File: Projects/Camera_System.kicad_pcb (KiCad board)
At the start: 2 copper layers, 67 x 98 mm, 63 parts, among them CON1 AVR-ISP-10, J1 BARREL_JACK, U1 IFX1117ME_V33, U10 RT1105AF160Q, U11 RT1105AF160Q, U12 LCD_1602, U13 RT1105AF160Q, U14 Si501, U15 OV7670-nofifo, U16 ESP8266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

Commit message: bom
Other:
- board size 67 x 98 mm -> 68 x 98 mm
- board text added: "A"
- board text added: "B"
- board text added: "CAMERA"
- board text added: "DISPLAY"
- board text added: "RST"
- board text added: "SD CARD"
- board text added: "WIFI"
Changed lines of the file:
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@@
     (links 191)
     (no_connects 0)
-    (area 52.324999 29.324999 271.775001 190.425001)
+    (area 40.024999 -48.28 278.375001 195.150001)
     (thickness 1.6)
-    (drawings 11)
+    (drawings 20)
     (tracks 659)
     (zones 0)
@@
     (visible_elements 7FFFFFFF)
     (pcbplotparams
-      (layerselection 0x00030_80000001)
+      (layerselection 0x01030_80000001)
       (usegerberextensions false)
       (excludeedgelayer true)
@@
       (psnegative false)
       (psa4output false)
-      (plotreference true)
-      (plotvalue true)
+      (plotreference false)
+      (plotvalue false)
       (plotinvisibletext false)
       (padsonsilk false)
@@
       (outputformat 1)
       (mirror false)
-      (drillshape 1)
+      (drillshape 0)
       (scaleselection 1)
-      (outputdirectory ""))
+      (outputdirectory Manufacturing/))
   )
   (net 0 "")
@@
     (tags "resistor 0603")
     (attr smd)
-    (fp_text reference R13 (at 0 -1.45) (layer F.SilkS)
+    (fp_text reference R13 (at 0.127 -1.524) (layer F.SilkS)
       (effects (font (size 1 1) (thickness 0.15)))
     )
@@
     (tags "resistor 0603")
     (attr smd)
-    (fp_text reference R10 (at 0 -1.45) (layer F.SilkS)
+    (fp_text reference R10 (at -0.081 1.546) (layer F.SilkS)
       (effects (font (size 1 1) (thickness 0.15)))
     )
@@
     (tags "resistor 0603")
     (attr smd)
-    (fp_text reference R9 (at 0 -1.45) (layer F.SilkS)
+    (fp_text reference R9 (at -0.208 -1.446) (layer F.SilkS)
       (effects (font (size 1 1) (thickness 0.15)))
     )
@@
     (tags "resistor 0603")
     (attr smd)
-    (fp_text reference R4 (at 0 -1.45 180) (layer F.SilkS)
+    (fp_text reference R4 (at 0.093 -1.858 180) (layer F.SilkS)
       (effects (font (size 1 1) (thickness 0.15)))
     )
@@
     (tags "resistor 0603")
     (attr smd)
-    (fp_text reference R2 (at 0 -1.45 270) (layer F.SilkS)
+    (fp_text reference R2 (at -0.351 -1.912 270) (layer F.SilkS)
       (effects (font (size 1 1) (thickness 0.15)))
     )
@@
     (tags "LED led 0603 SMD smd SMT smt smdled SMDLED smtled SMTLED")
     (attr smd)
-    (fp_text reference D3 (at 0 -1.25) (layer F.SilkS)
+    (fp_text reference D3 (at 0.13 1.858) (layer F.SilkS)
       (effects (font (size 1 1) (thickness 0.15)))
     )
@@
     (tags "LED led 0603 SMD smd SMT smt smdled SMDLED smtled SMTLED")
     (attr smd)
-    (fp_text reference D2 (at 0 -1.25 180) (layer F.SilkS)
+    (fp_text reference D2 (at -0.223 -2.041 180) (layer F.SilkS)
       (effects (font (size 1 1) (thickness 0.15)))
     )
@@
   (module MyLibraries:LD2980ABM50TR (layer F.Cu)
     (at 102.84 46.94 270)
-    (fp_text reference U2 (at 0.025 2.2 270) (layer F.SilkS)
+    (fp_text reference U2 (at 2.576 -1.025 360) (layer F.SilkS)
       (effects (font (size 1 1) (thickness 0.15)))
     )
@@
   (module MyLibraries:CS3M (layer F.Cu)
     (at 92.59 39.62 180)
-    (fp_text reference D1 (at 3.875 3.8 180) (layer F.SilkS)
+    (fp_text reference D1 (at 3.33 2.677 180) (layer F.SilkS)
       (effects (font (size 1 1) (thickness 0.15)))
     )
@@
     (tags "capacitor 0805")
     (attr smd)
-    (fp_text reference C5 (at 0 -1.75 180) (layer F.SilkS)
+    (fp_text reference C5 (at 1.25 -2.062 180) (layer F.SilkS)
       (effects (font (size 1 1) (thickness 0.15)))
     )
@@
     (tags "capacitor 0603")
     (attr smd)
-    (fp_text reference C4 (at 0 -1.25 180) (layer F.SilkS)
+    (fp_text reference C4 (at 1.556 -1.926 180) (layer F.SilkS)
       (effects (font (size 1 1) (thickness 0.15)))
     )
@@
     (tags "capacitor 0603")
     (attr smd)
-    (fp_text reference C3 (at 0 -1.25 180) (layer F.SilkS)
+    (fp_text reference C3 (at 1.016 -1.778 180) (layer F.SilkS)
       (effects (font (size 1 1) (thickness 0.15)))
     )
@@
   (module MyLibraries:UWX1E100MCL1GB (layer F.Cu)
     (at 92.03 47.73 270)
-    (fp_text reference C2 (at 0.175 5.575 270) (layer F.SilkS)
+    (fp_text reference C2 (at -1.897 2.516 360) (layer F.SilkS)
       (effects (font (size 1 1) (thickness 0.15)))
     )
@@
   (module MyLibraries:UWT1E470MCL6GS (layer F.Cu)
     (at 97.93 39.62 180)
-    (fp_text reference C1 (at 0.475 7.15 180) (layer F.SilkS)
+    (fp_text reference C1 (at -4.284 2.296 180) (layer F.SilkS)
       (effects (font (size 1 1) (thickness 0.15)))
     )
@@
       (net 12 /SCK))
   )
+  (dimension 98.044 (width 0.3) (layer B.Paste)
+    (gr_text "98.044 mm" (at 150.554 81.012 90) (layer B.Paste)
+      (effects (font (size 1.5 1.5) (thickness 0.3)))
+    )
+    (feature1 (pts (xy 139.044 31.99) (xy 151.904 31.99)))
+    (feature2 (pts (xy 139.044 130.034) (xy 151.904 130.034)))
+    (crossbar (pts (xy 149.204 130.034) (xy 149.204 31.99)))
+    (arrow1a (pts (xy 149.204 31.99) (xy 149.790421 33.116504)))
+    (arrow1b (pts (xy 149.204 31.99) (xy 148.617579 33.116504)))
+    (arrow2a (pts (xy 149.204 130.034) (xy 149.790421 128.907496)))
+    (arrow2b (pts (xy 149.204 130.034) (xy 148.617579 128.907496)))
+  )
+  (dimension 68.072 (width 0.3) (layer B.Paste)
+    (gr_text "68.072 mm" (at 105.008 138.241999) (layer B.Paste)
+      (effects (font (size 1.5 1.5) (thickness 0.3)))
+    )
+    (feature1 (pts (xy 139.044 130.034) (xy 139.044 139.591999)))
+    (feature2 (pts (xy 70.972 130.034) (xy 70.972 139.591999)))
+    (crossbar (pts (xy 70.972 136.891999) (xy 139.044 136.891999)))
+    (arrow1a (pts (xy 139.044 136.891999) (xy 137.917496 137.47842)))
+    (arrow1b (pts (xy 139.044 136.891999) (xy 137.917496 136.305578)))
+    (arrow2a (pts (xy 70.972 136.891999) (xy 72.098504 137.47842)))
+    (arrow2b (pts (xy 70.972 136.891999) (xy 72.098504 136.305578)))
+  )
+  (gr_text B (at 123.804 53.961 90) (layer F.SilkS)
+    (effects (font (size 1 1) (thickness 0.2)))
+  )
+  (gr_text A (at 106.532 53.834 90) (layer F.SilkS)
+    (effects (font (size 1 1) (thickness 0.2)))
+  )
+  (gr_text DISPLAY (at 107.675 36.054 90) (layer F.SilkS)
+    (effects (font (size 1 1) (thickness 0.2)))
+  )
+  (gr_text CAMERA (at 137.139 103.999 90) (layer F.SilkS)
+    (effects (font (size 1 1) (thickness 0.2)))
+  )
+  (gr_text WIFI (at 100.436 126.605 90) (layer F.SilkS)
+    (effects (font (size 1 1) (thickness 0.2)))
+  )
+  (gr_text "SD CARD" (at 77.449 96.506 90) (layer F.SilkS)
+    (effects (font (size 1 1) (thickness 0.2)))
+  )
+  (gr_text RST (at 81.132 120.636) (layer F.SilkS)
+    (effects (font (size 1 1) (thickness 0.2)))
+  )
   (gr_text SCK (at 97.15 84.84) (layer F.SilkS)
     (effects (font (size 1 1) (thickness 0.2)))
@@
     (effects (font (size 1 1) (thickness 0.2)))
   )
-  (gr_line (start 71 32) (end 138 32) (angle 90) (layer Edge.Cuts) (width 0.15))
+  (gr_line (start 71 32) (end 139 32) (angle 90) (layer Edge.Cuts) (width 0.15))
   (gr_line (start 71 130) (end 71 32) (angle 90) (layer Edge.Cuts) (width 0.15))
-  (gr_line (start 138 130) (end 71 130) (angle 90) (layer Edge.Cuts) (width 0.15))
-  (gr_line (start 138 32) (end 138 130) (angle 90) (layer Edge.Cuts) (width 0.15))
+  (gr_line (start 139 130) (end 71 130) (angle 90) (layer Edge.Cuts) (width 0.15))
+  (gr_line (start 139 32) (end 139 130) (angle 90) (layer Edge.Cuts) (width 0.15))
   (segment (start 110.9 96.96) (end 111.9 96.96) (width 0.25) (layer F.Cu) (net 0))
   (segment (start 113.9 96.99) (end 113.9 97) (width 0.25) (layer B.Cu) (net 0))

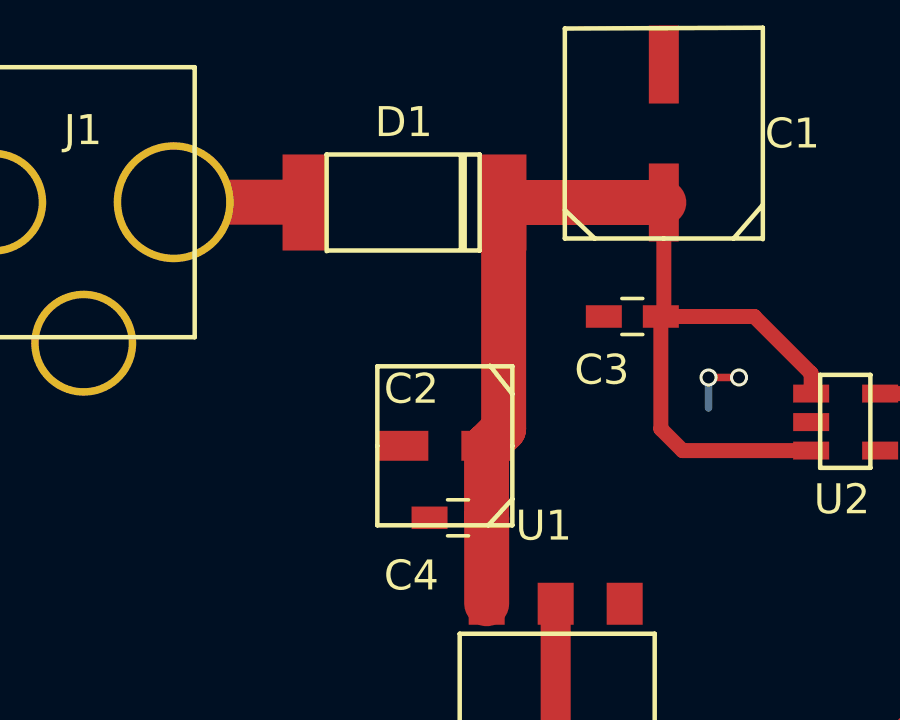
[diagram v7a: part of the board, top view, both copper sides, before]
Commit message: BOM has been updated and the items added to the mouser website
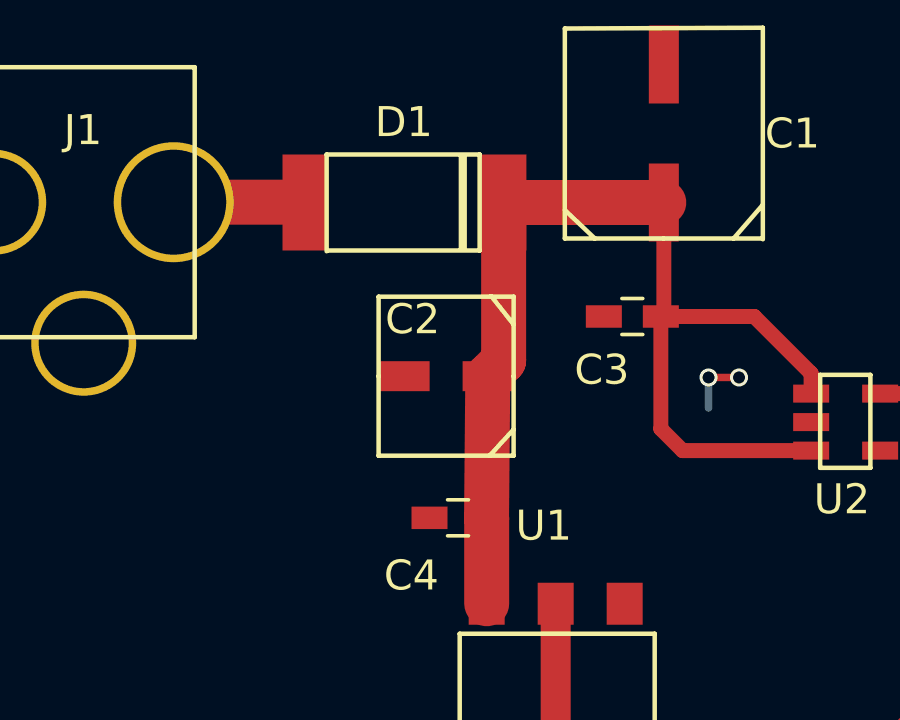
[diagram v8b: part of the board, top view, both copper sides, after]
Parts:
- moved C2 2.32 mm to (92.1, 45.4)
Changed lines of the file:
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@@
   )
   (setup
-    (last_trace_width 0.25)
+    (last_trace_width 1.5)
     (user_trace_width 0.5)
     (user_trace_width 1)
@@
   )
   (module MyLibraries:UWX1E100MCL1GB (layer F.Cu)
-    (at 92.03 47.73 270)
+    (at 92.072 45.41 270)
     (fp_text reference C2 (at -1.897 2.516 360) (layer F.SilkS)
       (effects (font (size 1 1) (thickness 0.15)))
@@
   (segment (start 94.325 52.995) (end 94.325 58.195) (width 1) (layer F.Cu) (net 2))
   (segment (start 122.42 122.66) (end 122.43 122.65) (width 1) (layer F.Cu) (net 2))
+  (segment (start 92.59 39.62) (end 92.59 44.892) (width 1.5) (layer F.Cu) (net 3) (status 400000))
+  (segment (start 92.59 44.892) (end 92.072 45.41) (width 1.5) (layer F.Cu) (net 3) (status 800000))
+  (segment (start 92.59 39.62) (end 97.93 39.62) (width 1.5) (layer F.Cu) (net 3) (status C00000))
   (segment (start 102.84 47.89) (end 98.556 47.89) (width 0.5) (layer F.Cu) (net 3))
   (segment (start 97.83 47.164) (end 97.83 43.42) (width 0.5) (layer F.Cu) (net 3))
@@
   (segment (start 97.93 43.32) (end 97.83 43.42) (width 0.5) (layer F.Cu) (net 3))
   (segment (start 97.93 43.26) (end 97.97 43.3) (width 0.5) (layer F.Cu) (net 3))
-  (segment (start 92.59 39.62) (end 97.93 39.62) (width 1.5) (layer F.Cu) (net 3))
-  (segment (start 92.59 39.62) (end 92.59 47.17) (width 1.5) (layer F.Cu) (net 3))
-  (segment (start 92.59 47.17) (end 92.03 47.73) (width 1.5) (layer F.Cu) (net 3))
-  (segment (start 92.02 50.13) (end 92.02 47.74) (width 1.5) (layer F.Cu) (net 3))
-  (segment (start 92.02 47.74) (end 92.03 47.73) (width 1.5) (layer F.Cu) (net 3))
+  (segment (start 92.02 50.13) (end 92.062 45.42) (width 1.5) (layer F.Cu) (net 3) (status 20))
+  (segment (start 92.062 45.42) (end 92.072 45.41) (width 1.5) (layer F.Cu) (net 3) (status 30))
   (segment (start 92.025 52.995) (end 92.025 50.135) (width 1.5) (layer F.Cu) (net 3))
   (segment (start 92.025 50.135) (end 92.02 50.13) (width 1.5) (layer F.Cu) (net 3))
